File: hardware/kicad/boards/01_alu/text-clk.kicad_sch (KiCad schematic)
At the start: 8 parts, among them U284 ICM7555xB, U285 74HCT541

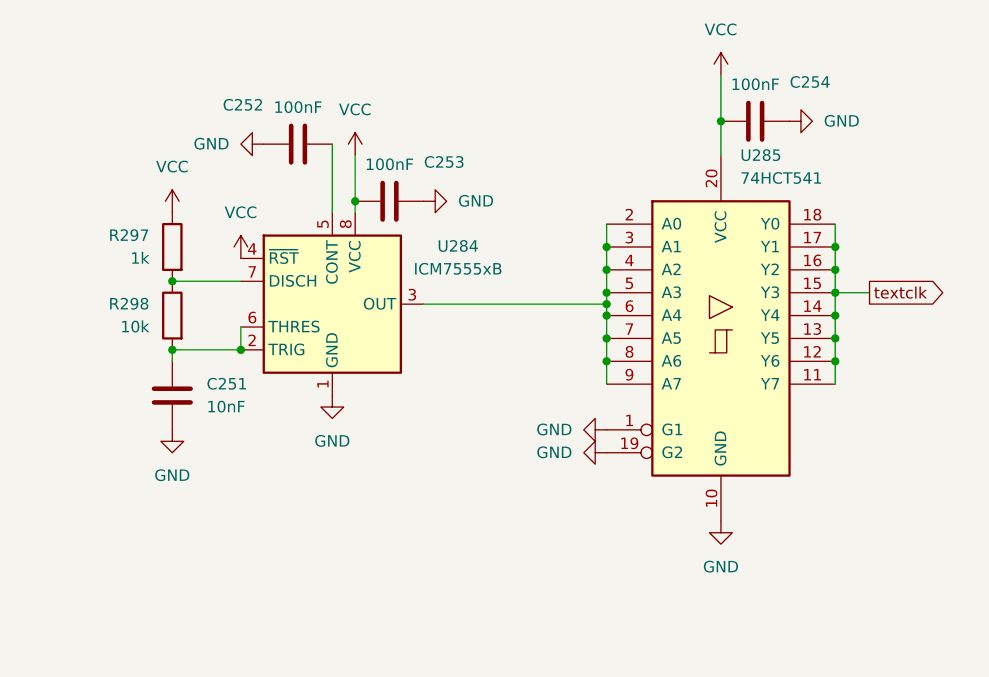
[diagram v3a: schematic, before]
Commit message: fix: fixed erc to 0; remaining are warnings about labeling which are being fixed; latest alu schematics pending decoration and organization
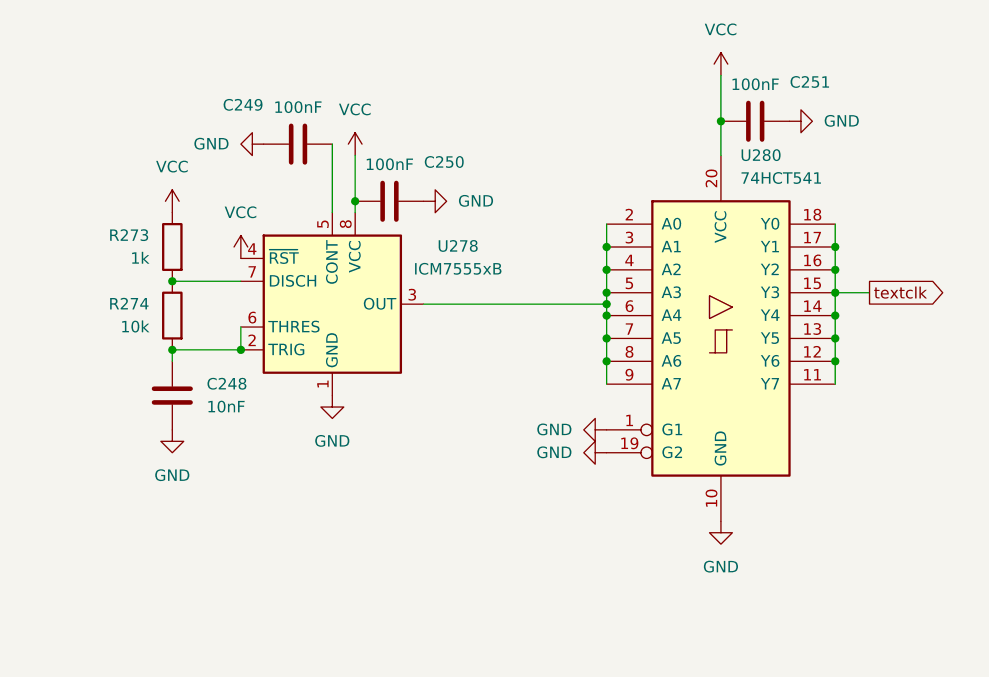
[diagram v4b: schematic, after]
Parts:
- renumbered C251 to C248, C252 to C249, C253 to C250, C254 to C251, R297 to R273, R298 to R274, U284 to U278, U285 to U280
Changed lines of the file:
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@@
 		(dnp no)
 		(fields_autoplaced yes)
-		(property "Reference" "#PWR01042"
+		(property "Reference" "#PWR01024"
 			(at 110.49 53.34 0)
 			(hide yes)
@@
 			(project "alu-32b"
 				(path "/ddad1417-0afc-402d-a021-92fc87ddd78a/70179ff6-7c16-4036-adf3-4ea9b5e0a238/259ce3bc-a28b-4687-b086-c0ff5aa711b4"
-					(reference "#PWR01042")
+					(reference "#PWR01024")
 					(unit 1)
 				)
@@
 		(dnp no)
 		(fields_autoplaced yes)
-		(property "Reference" "U285"
+		(property "Reference" "U280"
 			(at 173.5933 43.18 0)
 			(show_name no)
@@
 			(project "alu-32b"
 				(path "/ddad1417-0afc-402d-a021-92fc87ddd78a/70179ff6-7c16-4036-adf3-4ea9b5e0a238/259ce3bc-a28b-4687-b086-c0ff5aa711b4"
-					(reference "U285")
+					(reference "U280")
 					(unit 1)
 				)
@@
 		(dnp no)
 		(fields_autoplaced yes)
-		(property "Reference" "#PWR01045"
+		(property "Reference" "#PWR01027"
 			(at 114.3 41.91 0)
 			(hide yes)
@@
 			(project "alu-32b"
 				(path "/ddad1417-0afc-402d-a021-92fc87ddd78a/70179ff6-7c16-4036-adf3-4ea9b5e0a238/259ce3bc-a28b-4687-b086-c0ff5aa711b4"
-					(reference "#PWR01045")
+					(reference "#PWR01027")
 					(unit 1)
 				)
@@
 		(in_pos_files yes)
 		(dnp no)
-		(property "Reference" "C252"
+		(property "Reference" "C249"
 			(at 118.364 37.592 90)
 			(show_name no)
@@
 			(project "alu-32b"
 				(path "/ddad1417-0afc-402d-a021-92fc87ddd78a/70179ff6-7c16-4036-adf3-4ea9b5e0a238/259ce3bc-a28b-4687-b086-c0ff5aa711b4"
-					(reference "C252")
+					(reference "C249")
 					(unit 1)
 				)
@@
 		(in_pos_files yes)
 		(dnp no)
-		(property "Reference" "R297"
+		(property "Reference" "R273"
 			(at 107.95 52.0699 0)
 			(show_name no)
@@
 			(project "alu-32b"
 				(path "/ddad1417-0afc-402d-a021-92fc87ddd78a/70179ff6-7c16-4036-adf3-4ea9b5e0a238/259ce3bc-a28b-4687-b086-c0ff5aa711b4"
-					(reference "R297")
+					(reference "R273")
 					(unit 1)
 				)
@@
 		(dnp no)
 		(fields_autoplaced yes)
-		(property "Reference" "U284"
+		(property "Reference" "U278"
 			(at 142.24 53.2698 0)
 			(show_name no)
@@
 			(project "alu-32b"
 				(path "/ddad1417-0afc-402d-a021-92fc87ddd78a/70179ff6-7c16-4036-adf3-4ea9b5e0a238/259ce3bc-a28b-4687-b086-c0ff5aa711b4"
-					(reference "U284")
+					(reference "U278")
 					(unit 1)
 				)
@@
 		(dnp no)
 		(fields_autoplaced yes)
-		(property "Reference" "#PWR01046"
+		(property "Reference" "#PWR01028"
 			(at 128.27 76.2 0)
 			(hide yes)
@@
 			(project "alu-32b"
 				(path "/ddad1417-0afc-402d-a021-92fc87ddd78a/70179ff6-7c16-4036-adf3-4ea9b5e0a238/259ce3bc-a28b-4687-b086-c0ff5aa711b4"
-					(reference "#PWR01046")
+					(reference "#PWR01028")
 					(unit 1)
 				)
@@
 		(in_pos_files yes)
 		(dnp no)
-		(property "Reference" "C254"
+		(property "Reference" "C251"
 			(at 181.356 35.052 90)
 			(show_name no)
@@
 			(project "alu-32b"
 				(path "/ddad1417-0afc-402d-a021-92fc87ddd78a/70179ff6-7c16-4036-adf3-4ea9b5e0a238/259ce3bc-a28b-4687-b086-c0ff5aa711b4"
-					(reference "C254")
+					(reference "C251")
 					(unit 1)
 				)
@@
 		(in_pos_files yes)
 		(dnp no)
-		(property "Reference" "R298"
+		(property "Reference" "R274"
 			(at 107.95 59.6899 0)
 			(show_name no)
@@
 			(project "alu-32b"
 				(path "/ddad1417-0afc-402d-a021-92fc87ddd78a/70179ff6-7c16-4036-adf3-4ea9b5e0a238/259ce3bc-a28b-4687-b086-c0ff5aa711b4"
-					(reference "R298")
+					(reference "R274")
 					(unit 1)
 				)
@@
 		(dnp no)
 		(fields_autoplaced yes)
-		(property "Reference" "#PWR01044"
+		(property "Reference" "#PWR01026"
 			(at 118.11 58.42 0)
 			(hide yes)
@@
 			(project "alu-32b"
 				(path "/ddad1417-0afc-402d-a021-92fc87ddd78a/70179ff6-7c16-4036-adf3-4ea9b5e0a238/259ce3bc-a28b-4687-b086-c0ff5aa711b4"
-					(reference "#PWR01044")
+					(reference "#PWR01026")
 					(unit 1)
 				)
@@
 		(dnp no)
 		(fields_autoplaced yes)
-		(property "Reference" "#PWR01052"
+		(property "Reference" "#PWR01036"
 			(at 171.45 90.17 0)
 			(hide yes)
@@
 			(project "alu-32b"
 				(path "/ddad1417-0afc-402d-a021-92fc87ddd78a/70179ff6-7c16-4036-adf3-4ea9b5e0a238/259ce3bc-a28b-4687-b086-c0ff5aa711b4"
-					(reference "#PWR01052")
+					(reference "#PWR01036")
 					(unit 1)
 				)
@@
 		(dnp no)
 		(fields_autoplaced yes)
-		(property "Reference" "#PWR01050"
+		(property "Reference" "#PWR01034"
 			(at 152.4 76.2 0)
 			(hide yes)
@@
 			(project "alu-32b"
 				(path "/ddad1417-0afc-402d-a021-92fc87ddd78a/70179ff6-7c16-4036-adf3-4ea9b5e0a238/259ce3bc-a28b-4687-b086-c0ff5aa711b4"
-					(reference "#PWR01050")
+					(reference "#PWR01034")
 					(unit 1)
 				)
@@
 		(dnp no)
 		(fields_autoplaced yes)
-		(property "Reference" "#PWR01051"
+		(property "Reference" "#PWR01035"
 			(at 171.45 38.1 0)
 			(hide yes)
@@
 			(project "alu-32b"
 				(path "/ddad1417-0afc-402d-a021-92fc87ddd78a/70179ff6-7c16-4036-adf3-4ea9b5e0a238/259ce3bc-a28b-4687-b086-c0ff5aa711b4"
-					(reference "#PWR01051")
+					(reference "#PWR01035")
 					(unit 1)
 				)
@@
 		(dnp no)
 		(fields_autoplaced yes)
-		(property "Reference" "#PWR01048"
+		(property "Reference" "#PWR01030"
 			(at 144.78 48.26 0)
 			(hide yes)
@@
 			(project "alu-32b"
 				(path "/ddad1417-0afc-402d-a021-92fc87ddd78a/70179ff6-7c16-4036-adf3-4ea9b5e0a238/259ce3bc-a28b-4687-b086-c0ff5aa711b4"
-					(reference "#PWR01048")
+					(reference "#PWR01030")
 					(unit 1)
 				)
@@
 		(dnp no)
 		(fields_autoplaced yes)
-		(property "Reference" "#PWR01047"
+		(property "Reference" "#PWR01029"
 			(at 130.81 46.99 0)
 			(hide yes)
@@
 			(project "alu-32b"
 				(path "/ddad1417-0afc-402d-a021-92fc87ddd78a/70179ff6-7c16-4036-adf3-4ea9b5e0a238/259ce3bc-a28b-4687-b086-c0ff5aa711b4"
-					(reference "#PWR01047")
+					(reference "#PWR01029")
 					(unit 1)
 				)
@@
 		(dnp no)
 		(fields_autoplaced yes)
-		(property "Reference" "#PWR01049"
+		(property "Reference" "#PWR01033"
 			(at 152.4 73.66 0)
 			(hide yes)
@@
 			(project "alu-32b"
 				(path "/ddad1417-0afc-402d-a021-92fc87ddd78a/70179ff6-7c16-4036-adf3-4ea9b5e0a238/259ce3bc-a28b-4687-b086-c0ff5aa711b4"
-					(reference "#PWR01049")
+					(reference "#PWR01033")
 					(unit 1)
 				)
@@
 		(dnp no)
 		(fields_autoplaced yes)
-		(property "Reference" "#PWR01053"
+		(property "Reference" "#PWR01037"
 			(at 185.42 39.37 0)
 			(hide yes)
@@
 			(project "alu-32b"
 				(path "/ddad1417-0afc-402d-a021-92fc87ddd78a/70179ff6-7c16-4036-adf3-4ea9b5e0a238/259ce3bc-a28b-4687-b086-c0ff5aa711b4"
-					(reference "#PWR01053")
+					(reference "#PWR01037")
 					(unit 1)
 				)
@@
 		(dnp no)
 		(fields_autoplaced yes)
-		(property "Reference" "C251"
+		(property "Reference" "C248"
 			(at 114.3 68.5799 0)
 			(show_name no)
@@
 			(project "alu-32b"
 				(path "/ddad1417-0afc-402d-a021-92fc87ddd78a/70179ff6-7c16-4036-adf3-4ea9b5e0a238/259ce3bc-a28b-4687-b086-c0ff5aa711b4"
-					(reference "C251")
+					(reference "C248")
 					(unit 1)
 				)
@@
 		(in_pos_files yes)
 		(dnp no)
-		(property "Reference" "C253"
+		(property "Reference" "C250"
 			(at 140.716 43.942 90)
 			(show_name no)
@@
 			(project "alu-32b"
 				(path "/ddad1417-0afc-402d-a021-92fc87ddd78a/70179ff6-7c16-4036-adf3-4ea9b5e0a238/259ce3bc-a28b-4687-b086-c0ff5aa711b4"
-					(reference "C253")
+					(reference "C250")
 					(unit 1)
 				)
@@
 		(dnp no)
 		(fields_autoplaced yes)
-		(property "Reference" "#PWR01043"
+		(property "Reference" "#PWR01025"
 			(at 110.49 80.01 0)
 			(hide yes)
@@
 			(project "alu-32b"
 				(path "/ddad1417-0afc-402d-a021-92fc87ddd78a/70179ff6-7c16-4036-adf3-4ea9b5e0a238/259ce3bc-a28b-4687-b086-c0ff5aa711b4"
-					(reference "#PWR01043")
-					(unit 1)
-				)
+					(reference "#PWR01025")
+					(unit 1)
+				)

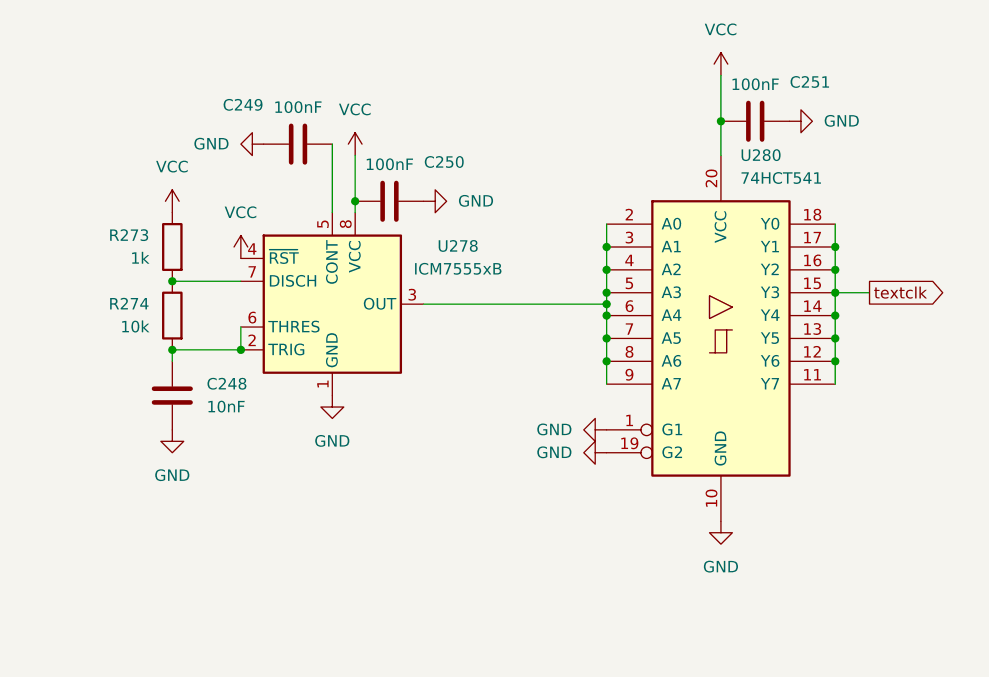
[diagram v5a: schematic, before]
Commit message: feat: designed ALU board with 0 ERC errors or warnings 🎉
Final review of logical correctness and footprints and then routing begins
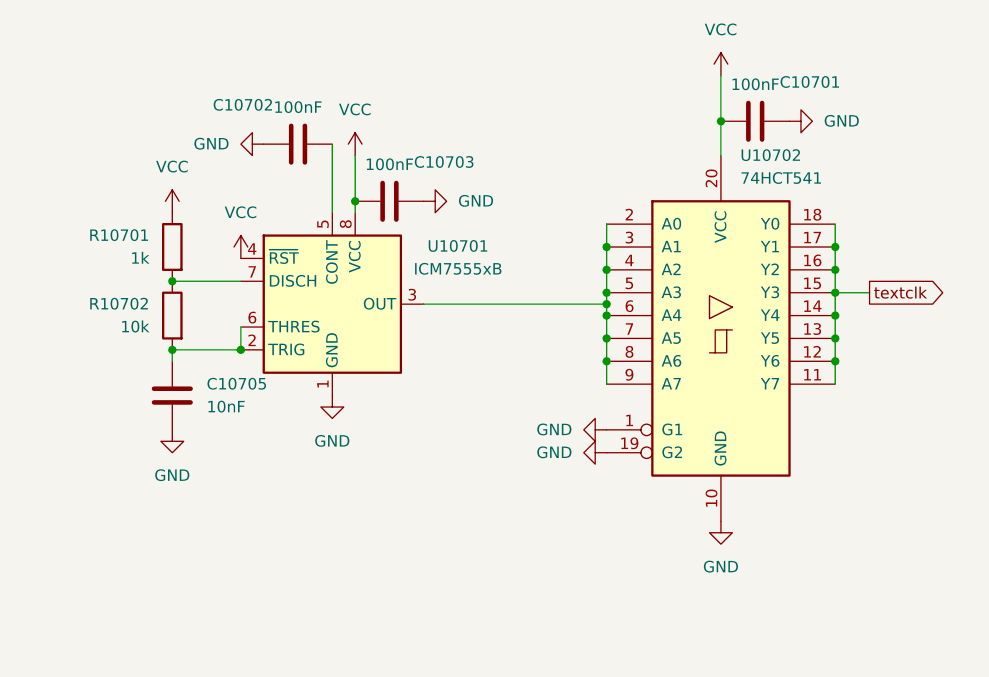
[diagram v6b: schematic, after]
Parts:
- renumbered C251 to C10701, C249 to C10702, C250 to C10703, C248 to C10705, R273 to R10701, R274 to R10702, U278 to U10701, U280 to U10702
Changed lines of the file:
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@@
 		(dnp no)
 		(fields_autoplaced yes)
-		(property "Reference" "#PWR01020"
+		(property "Reference" "#PWR010706"
 			(at 110.49 53.34 0)
 			(hide yes)
@@
 			(project "alu-32b"
 				(path "/ddad1417-0afc-402d-a021-92fc87ddd78a/70179ff6-7c16-4036-adf3-4ea9b5e0a238/259ce3bc-a28b-4687-b086-c0ff5aa711b4"
-					(reference "#PWR01020")
+					(reference "#PWR010706")
 					(unit 1)
 				)
@@
 		(dnp no)
 		(fields_autoplaced yes)
-		(property "Reference" "U280"
+		(property "Reference" "U10702"
 			(at 173.5933 43.18 0)
 			(show_name no)
@@
 			(project "alu-32b"
 				(path "/ddad1417-0afc-402d-a021-92fc87ddd78a/70179ff6-7c16-4036-adf3-4ea9b5e0a238/259ce3bc-a28b-4687-b086-c0ff5aa711b4"
-					(reference "U280")
+					(reference "U10702")
 					(unit 1)
 				)
@@
 		(dnp no)
 		(fields_autoplaced yes)
-		(property "Reference" "#PWR01023"
+		(property "Reference" "#PWR010703"
 			(at 114.3 41.91 0)
 			(hide yes)
@@
 			(project "alu-32b"
 				(path "/ddad1417-0afc-402d-a021-92fc87ddd78a/70179ff6-7c16-4036-adf3-4ea9b5e0a238/259ce3bc-a28b-4687-b086-c0ff5aa711b4"
-					(reference "#PWR01023")
+					(reference "#PWR010703")
 					(unit 1)
 				)
@@
 		(in_pos_files yes)
 		(dnp no)
-		(property "Reference" "C249"
+		(property "Reference" "C10702"
 			(at 118.364 37.592 90)
 			(show_name no)
@@
 			(project "alu-32b"
 				(path "/ddad1417-0afc-402d-a021-92fc87ddd78a/70179ff6-7c16-4036-adf3-4ea9b5e0a238/259ce3bc-a28b-4687-b086-c0ff5aa711b4"
-					(reference "C249")
+					(reference "C10702")
 					(unit 1)
 				)
@@
 		(in_pos_files yes)
 		(dnp no)
-		(property "Reference" "R273"
+		(property "Reference" "R10701"
 			(at 107.95 52.0699 0)
 			(show_name no)
@@
 			(project "alu-32b"
 				(path "/ddad1417-0afc-402d-a021-92fc87ddd78a/70179ff6-7c16-4036-adf3-4ea9b5e0a238/259ce3bc-a28b-4687-b086-c0ff5aa711b4"
-					(reference "R273")
+					(reference "R10701")
 					(unit 1)
 				)
@@
 		(dnp no)
 		(fields_autoplaced yes)
-		(property "Reference" "U278"
+		(property "Reference" "U10701"
 			(at 142.24 53.2698 0)
 			(show_name no)
@@
 			(project "alu-32b"
 				(path "/ddad1417-0afc-402d-a021-92fc87ddd78a/70179ff6-7c16-4036-adf3-4ea9b5e0a238/259ce3bc-a28b-4687-b086-c0ff5aa711b4"
-					(reference "U278")
+					(reference "U10701")
 					(unit 1)
 				)
@@
 		(dnp no)
 		(fields_autoplaced yes)
-		(property "Reference" "#PWR01024"
+		(property "Reference" "#PWR010710"
 			(at 128.27 76.2 0)
 			(hide yes)
@@
 			(project "alu-32b"
 				(path "/ddad1417-0afc-402d-a021-92fc87ddd78a/70179ff6-7c16-4036-adf3-4ea9b5e0a238/259ce3bc-a28b-4687-b086-c0ff5aa711b4"
-					(reference "#PWR01024")
+					(reference "#PWR010710")
 					(unit 1)
 				)
@@
 		(in_pos_files yes)
 		(dnp no)
-		(property "Reference" "C251"
+		(property "Reference" "C10701"
 			(at 181.356 35.052 90)
 			(show_name no)
@@
 			(project "alu-32b"
 				(path "/ddad1417-0afc-402d-a021-92fc87ddd78a/70179ff6-7c16-4036-adf3-4ea9b5e0a238/259ce3bc-a28b-4687-b086-c0ff5aa711b4"
-					(reference "C251")
+					(reference "C10701")
 					(unit 1)
 				)
@@
 		(in_pos_files yes)
 		(dnp no)
-		(property "Reference" "R274"
+		(property "Reference" "R10702"
 			(at 107.95 59.6899 0)
 			(show_name no)
@@
 			(project "alu-32b"
 				(path "/ddad1417-0afc-402d-a021-92fc87ddd78a/70179ff6-7c16-4036-adf3-4ea9b5e0a238/259ce3bc-a28b-4687-b086-c0ff5aa711b4"
-					(reference "R274")
+					(reference "R10702")
 					(unit 1)
 				)
@@
 		(dnp no)
 		(fields_autoplaced yes)
-		(property "Reference" "#PWR01022"
+		(property "Reference" "#PWR010707"
 			(at 118.11 58.42 0)
 			(hide yes)
@@
 			(project "alu-32b"
 				(path "/ddad1417-0afc-402d-a021-92fc87ddd78a/70179ff6-7c16-4036-adf3-4ea9b5e0a238/259ce3bc-a28b-4687-b086-c0ff5aa711b4"
-					(reference "#PWR01022")
+					(reference "#PWR010707")
 					(unit 1)
 				)
@@
 		(dnp no)
 		(fields_autoplaced yes)
-		(property "Reference" "#PWR01032"
+		(property "Reference" "#PWR010714"
 			(at 171.45 90.17 0)
 			(hide yes)
@@
 			(project "alu-32b"
 				(path "/ddad1417-0afc-402d-a021-92fc87ddd78a/70179ff6-7c16-4036-adf3-4ea9b5e0a238/259ce3bc-a28b-4687-b086-c0ff5aa711b4"
-					(reference "#PWR01032")
+					(reference "#PWR010714")
 					(unit 1)
 				)
@@
 		(dnp no)
 		(fields_autoplaced yes)
-		(property "Reference" "#PWR01030"
+		(property "Reference" "#PWR010713"
 			(at 152.4 76.2 0)
 			(hide yes)
@@
 			(project "alu-32b"
 				(path "/ddad1417-0afc-402d-a021-92fc87ddd78a/70179ff6-7c16-4036-adf3-4ea9b5e0a238/259ce3bc-a28b-4687-b086-c0ff5aa711b4"
-					(reference "#PWR01030")
+					(reference "#PWR010713")
 					(unit 1)
 				)
@@
 		(dnp no)
 		(fields_autoplaced yes)
-		(property "Reference" "#PWR01031"
+		(property "Reference" "#PWR010701"
 			(at 171.45 38.1 0)
 			(hide yes)
@@
 			(project "alu-32b"
 				(path "/ddad1417-0afc-402d-a021-92fc87ddd78a/70179ff6-7c16-4036-adf3-4ea9b5e0a238/259ce3bc-a28b-4687-b086-c0ff5aa711b4"
-					(reference "#PWR01031")
+					(reference "#PWR010701")
 					(unit 1)
 				)
@@
 		(dnp no)
 		(fields_autoplaced yes)
-		(property "Reference" "#PWR01026"
+		(property "Reference" "#PWR010705"
 			(at 144.78 48.26 0)
 			(hide yes)
@@
 			(project "alu-32b"
 				(path "/ddad1417-0afc-402d-a021-92fc87ddd78a/70179ff6-7c16-4036-adf3-4ea9b5e0a238/259ce3bc-a28b-4687-b086-c0ff5aa711b4"
-					(reference "#PWR01026")
+					(reference "#PWR010705")
 					(unit 1)
 				)
@@
 		(dnp no)
 		(fields_autoplaced yes)
-		(property "Reference" "#PWR01025"
+		(property "Reference" "#PWR010704"
 			(at 130.81 46.99 0)
 			(hide yes)
@@
 			(project "alu-32b"
 				(path "/ddad1417-0afc-402d-a021-92fc87ddd78a/70179ff6-7c16-4036-adf3-4ea9b5e0a238/259ce3bc-a28b-4687-b086-c0ff5aa711b4"
-					(reference "#PWR01025")
+					(reference "#PWR010704")
 					(unit 1)
 				)
@@
 		(dnp no)
 		(fields_autoplaced yes)
-		(property "Reference" "#PWR01029"
+		(property "Reference" "#PWR010712"
 			(at 152.4 73.66 0)
 			(hide yes)
@@
 			(project "alu-32b"
 				(path "/ddad1417-0afc-402d-a021-92fc87ddd78a/70179ff6-7c16-4036-adf3-4ea9b5e0a238/259ce3bc-a28b-4687-b086-c0ff5aa711b4"
-					(reference "#PWR01029")
+					(reference "#PWR010712")
 					(unit 1)
 				)
@@
 		(dnp no)
 		(fields_autoplaced yes)
-		(property "Reference" "#PWR01033"
+		(property "Reference" "#PWR010702"
 			(at 185.42 39.37 0)
 			(hide yes)
@@
 			(project "alu-32b"
 				(path "/ddad1417-0afc-402d-a021-92fc87ddd78a/70179ff6-7c16-4036-adf3-4ea9b5e0a238/259ce3bc-a28b-4687-b086-c0ff5aa711b4"
-					(reference "#PWR01033")
+					(reference "#PWR010702")
 					(unit 1)
 				)
@@
 		(dnp no)
 		(fields_autoplaced yes)
-		(property "Reference" "C248"
+		(property "Reference" "C10705"
 			(at 114.3 68.5799 0)
 			(show_name no)
@@
 			(project "alu-32b"
 				(path "/ddad1417-0afc-402d-a021-92fc87ddd78a/70179ff6-7c16-4036-adf3-4ea9b5e0a238/259ce3bc-a28b-4687-b086-c0ff5aa711b4"
-					(reference "C248")
+					(reference "C10705")
 					(unit 1)
 				)
@@
 		(in_pos_files yes)
 		(dnp no)
-		(property "Reference" "C250"
+		(property "Reference" "C10703"
 			(at 140.716 43.942 90)
 			(show_name no)
@@
 			(project "alu-32b"
 				(path "/ddad1417-0afc-402d-a021-92fc87ddd78a/70179ff6-7c16-4036-adf3-4ea9b5e0a238/259ce3bc-a28b-4687-b086-c0ff5aa711b4"
-					(reference "C250")
+					(reference "C10703")
 					(unit 1)
 				)
@@
 		(dnp no)
 		(fields_autoplaced yes)
-		(property "Reference" "#PWR01021"
+		(property "Reference" "#PWR010711"
 			(at 110.49 80.01 0)
 			(hide yes)
@@
 			(project "alu-32b"
 				(path "/ddad1417-0afc-402d-a021-92fc87ddd78a/70179ff6-7c16-4036-adf3-4ea9b5e0a238/259ce3bc-a28b-4687-b086-c0ff5aa711b4"
-					(reference "#PWR01021")
-					(unit 1)
-				)
+					(reference "#PWR010711")
+					(unit 1)
+				)
